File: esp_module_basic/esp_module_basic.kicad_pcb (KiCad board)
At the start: 2 copper layers, 19 parts, among them P1 CONN_01X4, P2 CONN_01X15, P3 CONN_01X15

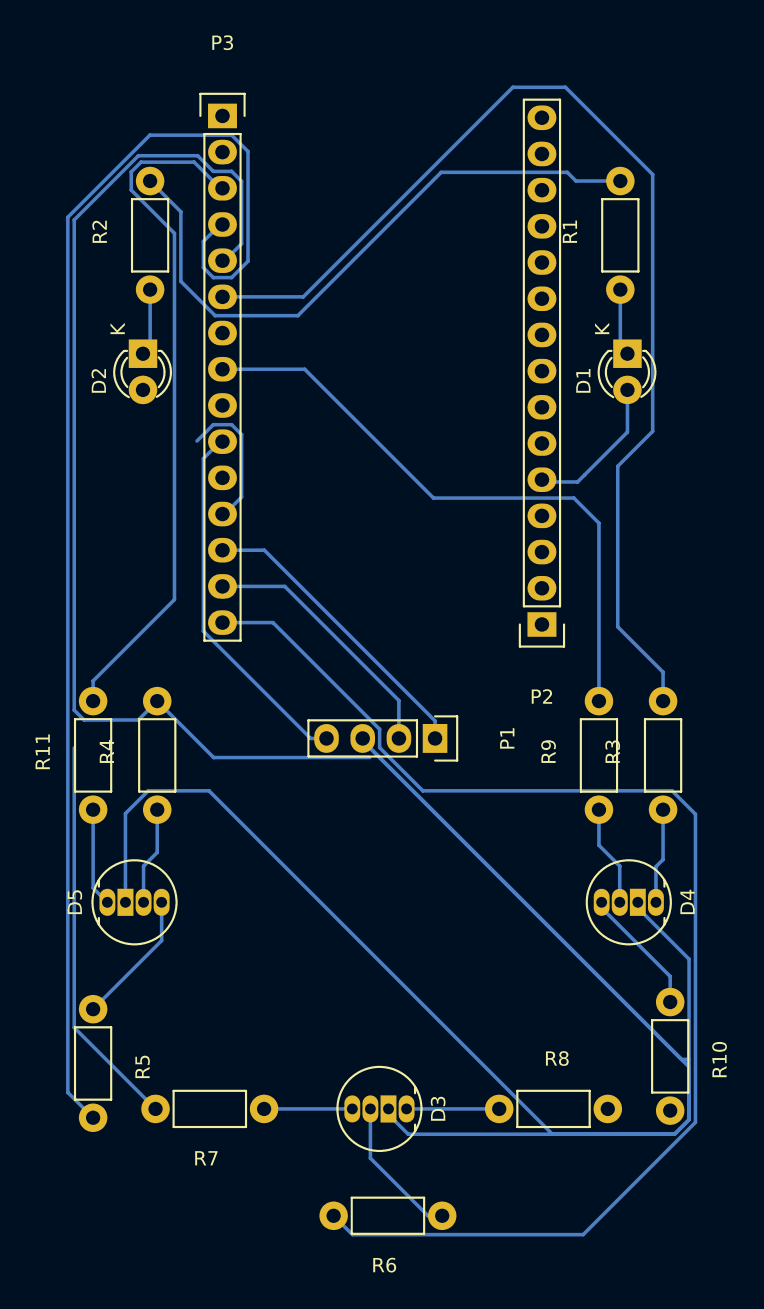
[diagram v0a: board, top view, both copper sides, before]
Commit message: Updated the PCB traces
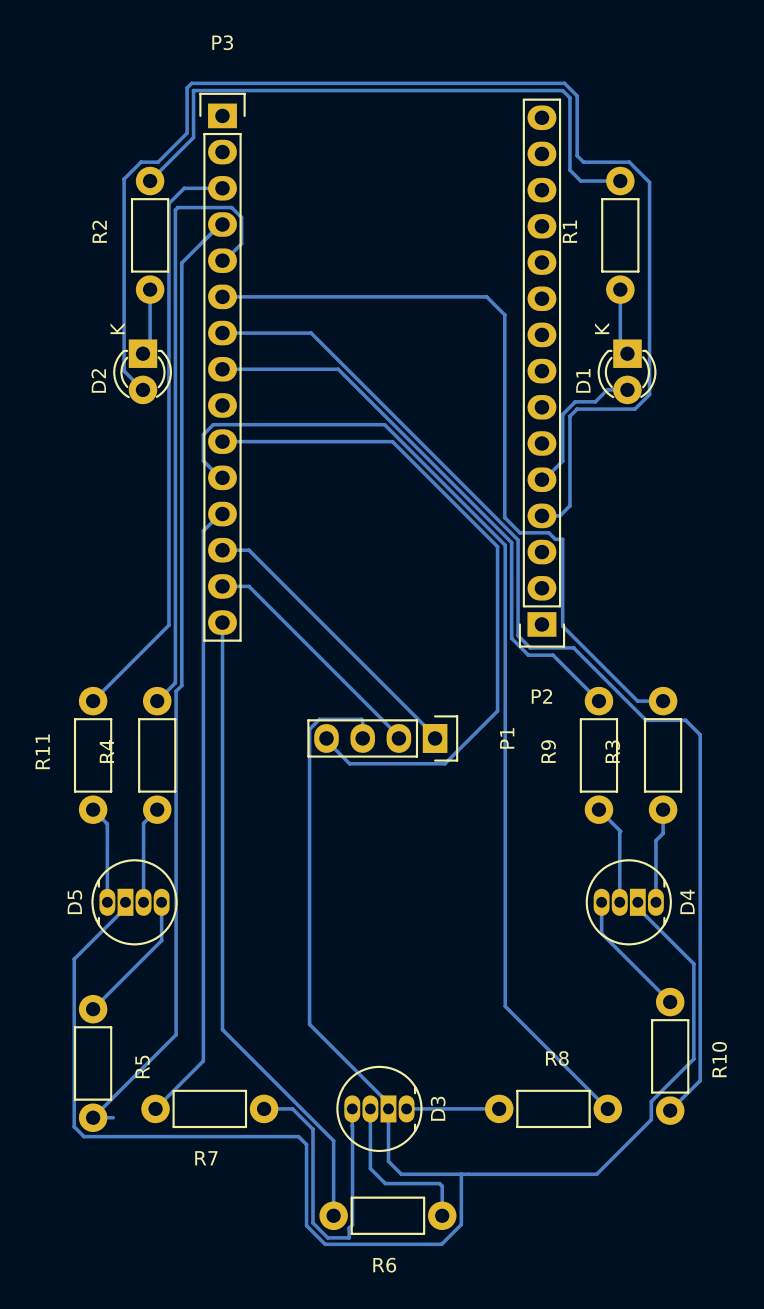
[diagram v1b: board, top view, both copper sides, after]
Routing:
- net sd3: track 0.00 -> 91.9 mm
- net d6: track 0.15 -> 76.5 mm
- net d4: track 0.00 -> 71.2 mm
- net d0: track 90.4 -> 44.9 mm
- net d8: track 78.2 -> 43.7 mm
- net GND: track 164.6 -> 132.3 mm
- net rx: track 94.7 -> 69.6 mm
- net d7: track 78.1 -> 54.6 mm
- net 3_3v: track 25.7 -> 48.6 mm
- net Net-(D3-Pad4): track 6.40 -> 23.4 mm
- net tx: track 48.2 -> 41.5 mm
- net d3: track 37.8 -> 43.9 mm
- net d5: track 43.4 -> 40.0 mm
- net Net-(D3-Pad3): track 10.2 -> 11.8 mm
- net d1: track 18.4 -> 16.9 mm
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
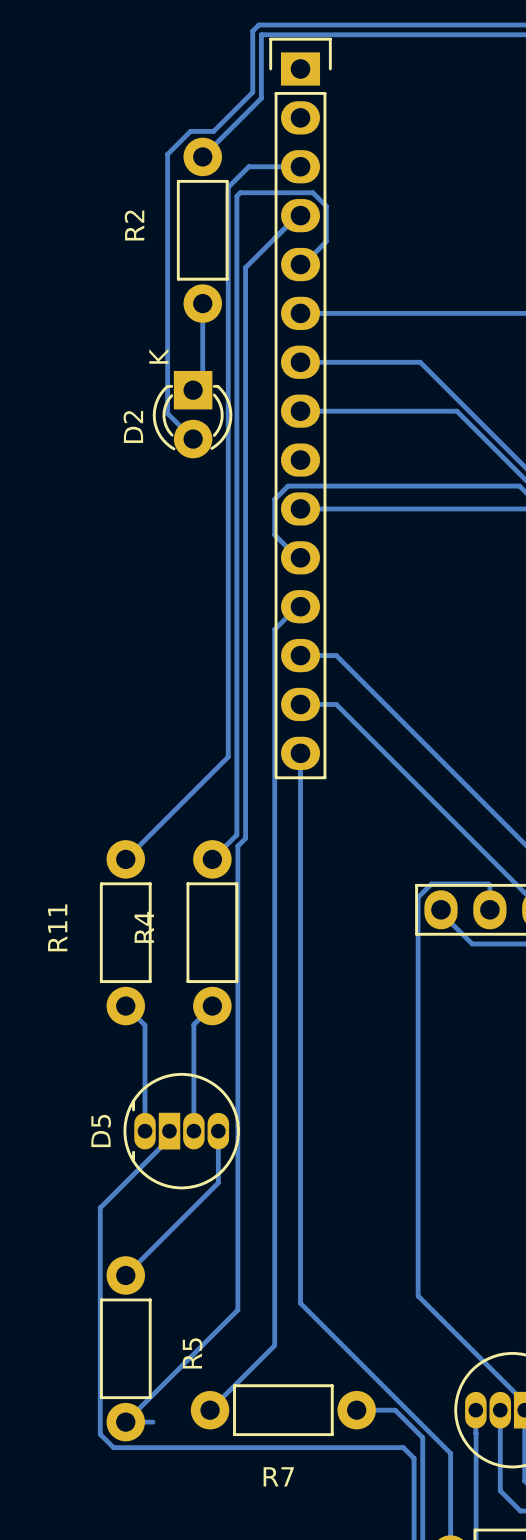
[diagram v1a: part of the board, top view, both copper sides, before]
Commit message: Fixing missing GND trace
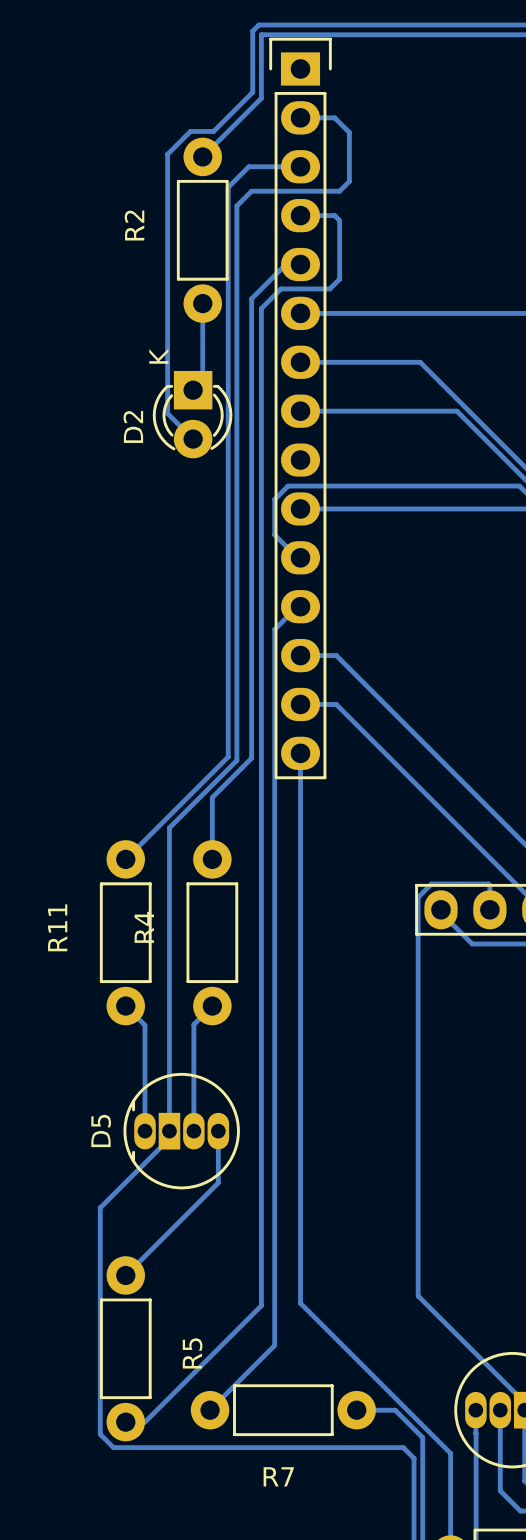
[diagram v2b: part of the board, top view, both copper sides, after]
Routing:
- net GND: track 132.3 -> 193.6 mm
- net d8: track 43.7 -> 33.4 mm
- net rx: track 69.6 -> 71.4 mm
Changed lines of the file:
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@@
   (general
     (links 35)
-    (no_connects 6)
+    (no_connects 5)
     (area 54.715 61.235 104.57512 149.07512)
     (thickness 1.6)
     (drawings 0)
-    (tracks 184)
+    (tracks 194)
     (zones 0)
     (modules 19)
@@
     (add_net tx)
   )
+  (module LEDs:LED-RGB-5MM_Common_Cathode (layer F.Cu)
+    (at 60.5 122.5 90)
+    (descr "5mm common cathode RGB LED")
+    (tags "RGB LED 5mm Common Cathode")
+    (fp_text reference D5 (at 0 -2.25 90) (layer F.SilkS)
+      (effects (font (size 1 1) (thickness 0.15)))
+    )
+    (fp_text value LED_RCBG (at 0 6.25 90) (layer F.Fab)
+      (effects (font (size 1 1) (thickness 0.15)))
+    )
+    (fp_circle (center 0 1.905) (end 3.2 1.905) (layer F.CrtYd) (width 0.05))
+    (fp_line (start -1.1 -0.595) (end -1.55 -0.595) (layer F.SilkS) (width 0.15))
+    (fp_circle (center 0 1.905) (end 2.95 1.905) (layer F.SilkS) (width 0.15))
+    (fp_line (start 1.1 -0.595) (end 1.55 -0.595) (layer F.SilkS) (width 0.15))
+    (pad 1 thru_hole oval (at 0 0 90) (size 1.905 1.1176) (drill 0.762) (layers *.Cu *.Mask F.SilkS)
+      (net 12 "Net-(D5-Pad1)"))
+    (pad 2 thru_hole rect (at 0 1.27 90) (size 1.905 1.1176) (drill 0.762) (layers *.Cu *.Mask F.SilkS)
+      (net 7 GND))
+    (pad 3 thru_hole oval (at 0 2.54 90) (size 1.905 1.1176) (drill 0.762) (layers *.Cu *.Mask F.SilkS)
+      (net 13 "Net-(D5-Pad3)"))
+    (pad 4 thru_hole oval (at 0 3.81 90) (size 1.905 1.1176) (drill 0.762) (layers *.Cu *.Mask F.SilkS)
+      (net 14 "Net-(D5-Pad4)"))
+  )
   (module LEDs:LED-3MM (layer F.Cu)
     (at 97 84 270)
@@
     (pad 4 thru_hole oval (at 0 3.81 270) (size 1.905 1.1176) (drill 0.762) (layers *.Cu *.Mask F.SilkS)
       (net 11 "Net-(D4-Pad4)"))
-  )
-  (module LEDs:LED-RGB-5MM_Common_Cathode (layer F.Cu)
-    (at 60.5 122.5 90)
-    (descr "5mm common cathode RGB LED")
-    (tags "RGB LED 5mm Common Cathode")
-    (fp_text reference D5 (at 0 -2.25 90) (layer F.SilkS)
-      (effects (font (size 1 1) (thickness 0.15)))
-    )
-    (fp_text value LED_RCBG (at 0 6.25 90) (layer F.Fab)
-      (effects (font (size 1 1) (thickness 0.15)))
-    )
-    (fp_circle (center 0 1.905) (end 3.2 1.905) (layer F.CrtYd) (width 0.05))
-    (fp_line (start -1.1 -0.595) (end -1.55 -0.595) (layer F.SilkS) (width 0.15))
-    (fp_circle (center 0 1.905) (end 2.95 1.905) (layer F.SilkS) (width 0.15))
-    (fp_line (start 1.1 -0.595) (end 1.55 -0.595) (layer F.SilkS) (width 0.15))
-    (pad 1 thru_hole oval (at 0 0 90) (size 1.905 1.1176) (drill 0.762) (layers *.Cu *.Mask F.SilkS)
-      (net 12 "Net-(D5-Pad1)"))
-    (pad 2 thru_hole rect (at 0 1.27 90) (size 1.905 1.1176) (drill 0.762) (layers *.Cu *.Mask F.SilkS)
-      (net 7 GND))
-    (pad 3 thru_hole oval (at 0 2.54 90) (size 1.905 1.1176) (drill 0.762) (layers *.Cu *.Mask F.SilkS)
-      (net 13 "Net-(D5-Pad3)"))
-    (pad 4 thru_hole oval (at 0 3.81 90) (size 1.905 1.1176) (drill 0.762) (layers *.Cu *.Mask F.SilkS)
-      (net 14 "Net-(D5-Pad4)"))
   )
   (module Pin_Headers:Pin_Header_Straight_1x04 (layer F.Cu)
@@
   (segment (start 78.96 141.19) (end 78.96 137) (width 0.25) (layer B.Cu) (net 6))
   (segment (start 83.82 142.24) (end 80.01 142.24) (width 0.25) (layer B.Cu) (net 6))
+  (segment (start 61.77 122.5) (end 61.77 106.746398) (width 0.25) (layer B.Cu) (net 7) (status 400000))
+  (segment (start 70.358 69.85) (end 68.58 69.85) (width 0.25) (layer B.Cu) (net 7) (status 800000))
+  (segment (start 71.12 70.612) (end 70.358 69.85) (width 0.25) (layer B.Cu) (net 7))
+  (segment (start 71.12 73.152) (end 71.12 70.612) (width 0.25) (layer B.Cu) (net 7))
+  (segment (start 70.612 73.66) (end 71.12 73.152) (width 0.25) (layer B.Cu) (net 7))
+  (segment (start 66.04 73.66) (end 70.612 73.66) (width 0.25) (layer B.Cu) (net 7))
+  (segment (start 65.274493 74.425507) (end 66.04 73.66) (width 0.25) (layer B.Cu) (net 7))
+  (segment (start 65.274493 103.241905) (end 65.274493 74.425507) (width 0.25) (layer B.Cu) (net 7))
+  (segment (start 61.77 106.746398) (end 65.274493 103.241905) (width 0.25) (layer B.Cu) (net 7))
   (segment (start 78.42 111) (end 78.42 109.734) (width 0.25) (layer B.Cu) (net 7))
   (segment (start 78.42 109.734) (end 78.34499 109.65899) (width 0.25) (layer B.Cu) (net 7))
@@
   (segment (start 64.824491 103.055509) (end 64.824491 73.460491) (width 0.25) (layer B.Cu) (net 28))
   (segment (start 68.4276 72.39) (end 68.58 72.39) (width 0.25) (layer B.Cu) (net 28))
-  (segment (start 65.724511 107.291899) (end 65.724511 77.633089) (width 0.25) (layer B.Cu) (net 29))
-  (segment (start 65.724511 77.633089) (end 68.4276 74.93) (width 0.25) (layer B.Cu) (net 29))
+  (segment (start 59.5 137.62) (end 60.5 137.62) (width 0.25) (layer B.Cu) (net 29) (status 400000))
+  (segment (start 70.358 74.93) (end 68.58 74.93) (width 0.25) (layer B.Cu) (net 29) (status 800000))
+  (segment (start 70.612 75.184) (end 70.358 74.93) (width 0.25) (layer B.Cu) (net 29))
+  (segment (start 70.612 78.232) (end 70.612 75.184) (width 0.25) (layer B.Cu) (net 29))
+  (segment (start 70.104 78.74) (end 70.612 78.232) (width 0.25) (layer B.Cu) (net 29))
+  (segment (start 67.564 78.74) (end 70.104 78.74) (width 0.25) (layer B.Cu) (net 29))
+  (segment (start 66.548 79.756) (end 67.564 78.74) (width 0.25) (layer B.Cu) (net 29))
+  (segment (start 66.548 131.572) (end 66.548 79.756) (width 0.25) (layer B.Cu) (net 29))
+  (segment (start 60.5 137.62) (end 66.548 131.572) (width 0.25) (layer B.Cu) (net 29))
   (segment (start 68.4276 74.93) (end 68.58 74.93) (width 0.25) (layer B.Cu) (net 29))
-  (segment (start 59.5 137.62) (end 65.324491 131.795509) (width 0.25) (layer B.Cu) (net 29))
-  (segment (start 65.324491 131.795509) (end 65.324491 107.691919) (width 0.25) (layer B.Cu) (net 29))
-  (segment (start 65.324491 107.691919) (end 65.724511 107.291899) (width 0.25) (layer B.Cu) (net 29))
-  (segment (start 59.5 137.62) (end 60.913492 137.62) (width 0.25) (layer B.Cu) (net 29))
-  (segment (start 67.23899 76.11861) (end 68.4276 74.93) (width 0.25) (layer B.Cu) (net 29))
-  (segment (start 64 108.38) (end 65.274501 107.105499) (width 0.25) (layer B.Cu) (net 30))
-  (segment (start 65.274501 107.105499) (end 65.274501 73.917499) (width 0.25) (layer B.Cu) (net 30))
+  (segment (start 65.532 103.632) (end 66.04 103.124) (width 0.25) (layer B.Cu) (net 30))
+  (segment (start 64 105.164) (end 65.532 103.632) (width 0.25) (layer B.Cu) (net 30))
+  (segment (start 64 108.38) (end 64 105.164) (width 0.25) (layer B.Cu) (net 30) (status 400000))
+  (segment (start 66.04 79.248) (end 67.818 77.47) (width 0.25) (layer B.Cu) (net 30) (status 800000))
+  (segment (start 66.04 103.124) (end 66.04 79.248) (width 0.25) (layer B.Cu) (net 30))
+  (segment (start 67.818 77.47) (end 68.58 77.47) (width 0.25) (layer B.Cu) (net 30) (status C00000))
   (segment (start 68.7324 77.47) (end 68.58 77.47) (width 0.25) (layer B.Cu) (net 30))
-  (segment (start 65.274501 73.917499) (end 65.45061 73.74139) (width 0.25) (layer B.Cu) (net 30))
-  (segment (start 65.45061 73.74139) (end 69.224738 73.74139) (width 0.25) (layer B.Cu) (net 30))
-  (segment (start 69.224738 73.74139) (end 69.92101 74.437662) (width 0.25) (layer B.Cu) (net 30))
-  (segment (start 69.92101 74.437662) (end 69.92101 76.28139) (width 0.25) (layer B.Cu) (net 30))
-  (segment (start 69.92101 76.28139) (end 68.7324 77.47) (width 0.25) (layer B.Cu) (net 30))
   (segment (start 88.392 81.28) (end 87.122 80.01) (width 0.25) (layer B.Cu) (net 31))
   (segment (start 87.122 80.01) (end 68.58 80.01) (width 0.25) (layer B.Cu) (net 31))

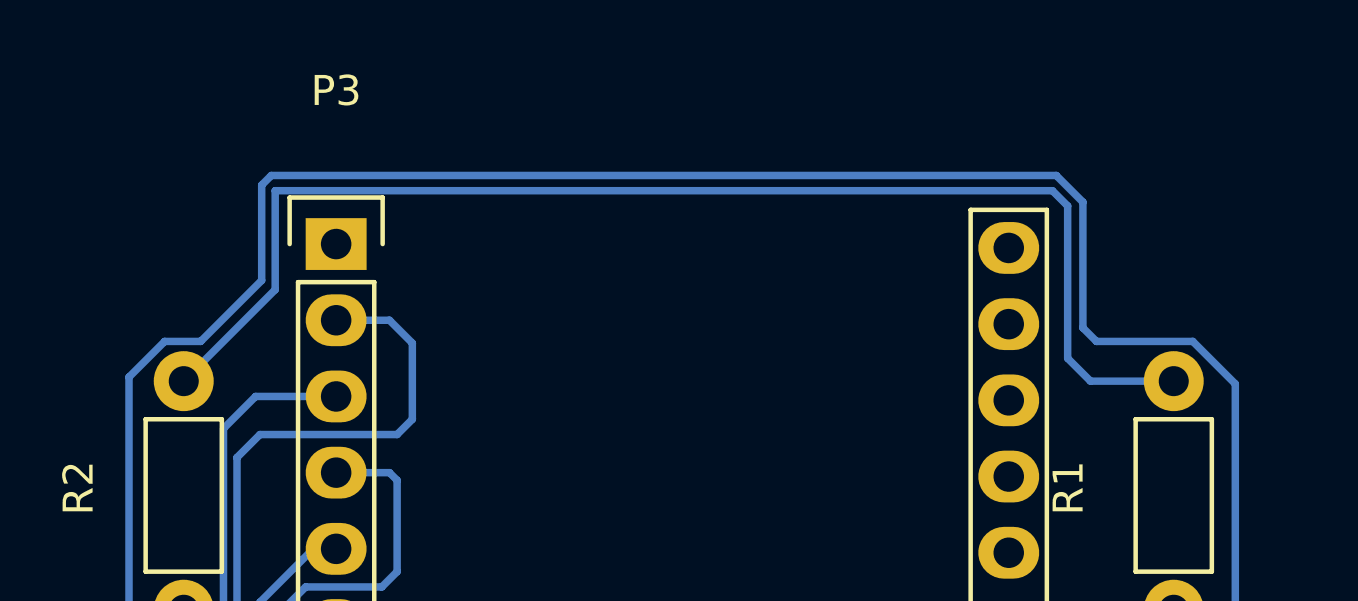
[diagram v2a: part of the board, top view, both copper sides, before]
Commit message: fix ground connection and fix labels for shared unconnected pins
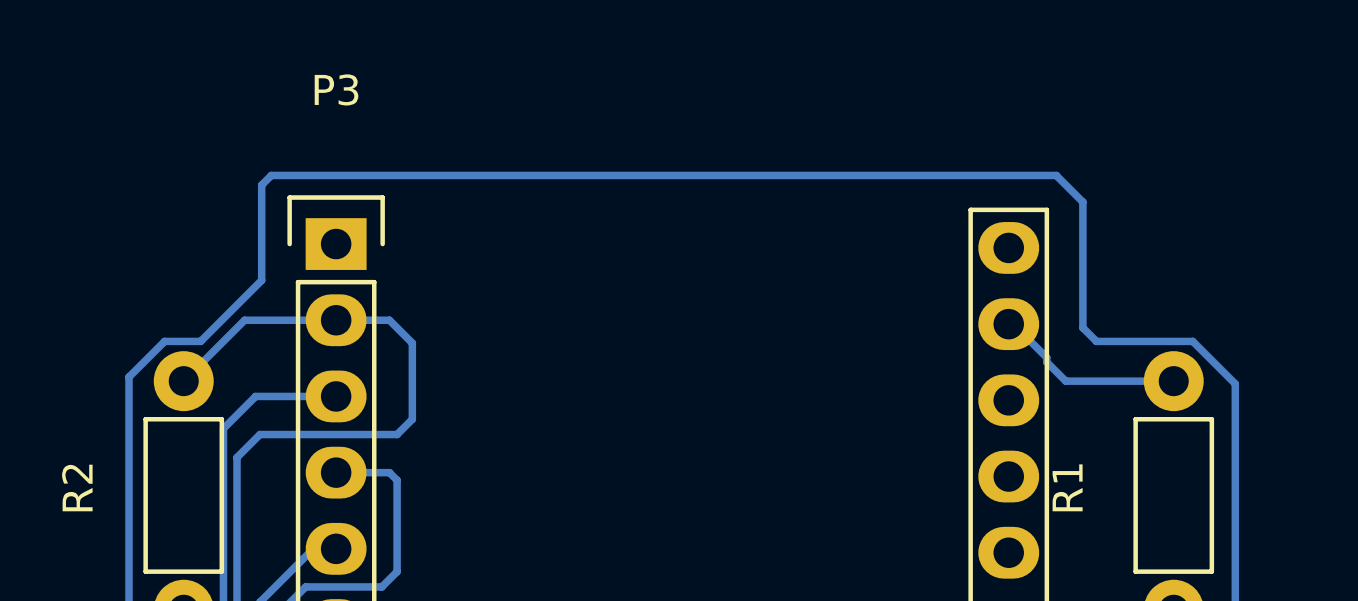
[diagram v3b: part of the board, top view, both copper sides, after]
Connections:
- D3 pad 2: GND -> GND_2
- D4 pad 2: GND -> GND_2
- D5 pad 2: GND -> GND_2
- P1 pad 3: GND -> GND_2
- P2 pad 10: GND -> GND_10
- P2 pad 14: GND -> GND_14
- P3 pad 1: 3_3v -> Net-(P3-Pad1)
- P3 pad 2: GND -> GND_2
- P3 pad 9: GND -> GND_9
- R1 pad 2: Net-(R1-Pad2) -> GND_14
- R2 pad 2: Net-(R1-Pad2) -> GND_2
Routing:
- net GND_2: track 0.00 -> 199.5 mm
- net GND: track 193.6 -> 0.00 mm
- net Net-(R1-Pad2): track 43.2 -> 0.00 mm
- net GND_14: track 0.00 -> 6.38 mm
